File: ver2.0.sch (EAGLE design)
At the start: 57 parts

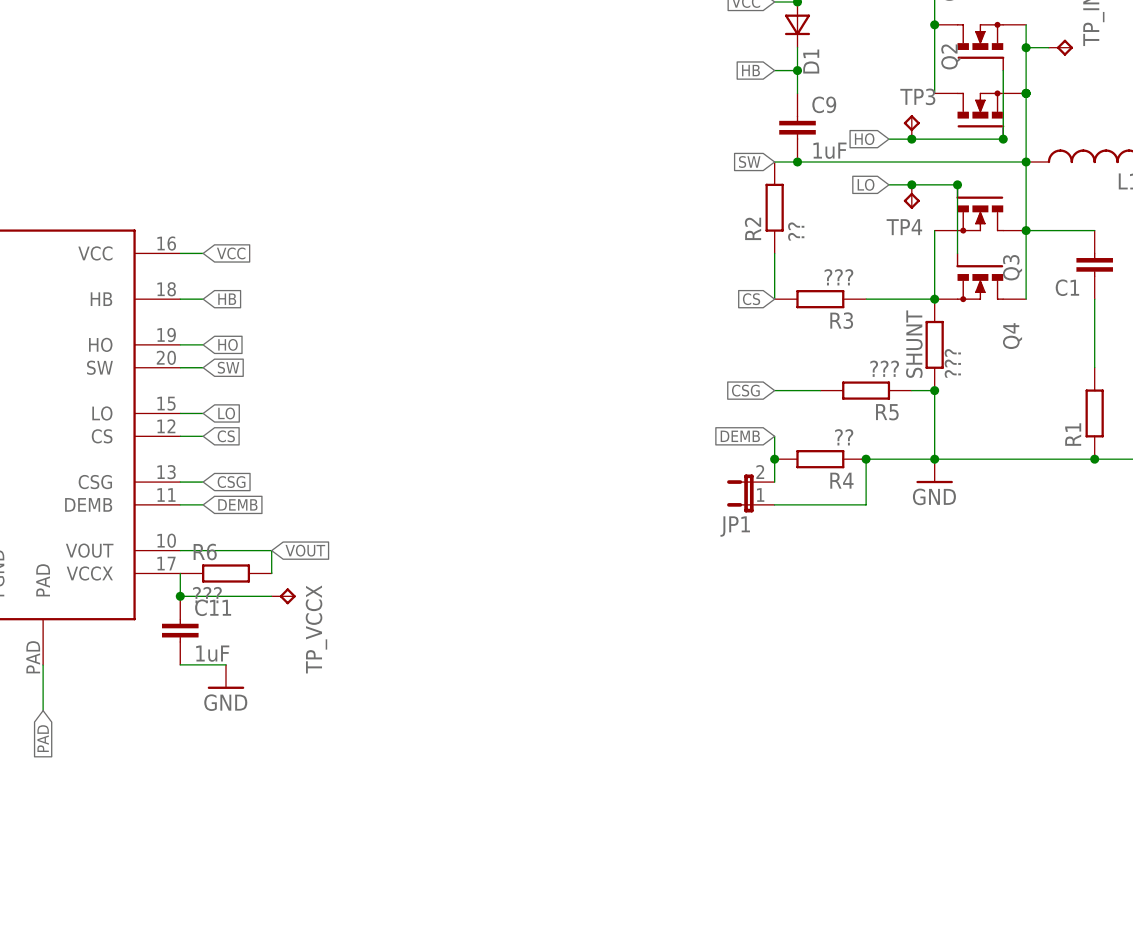
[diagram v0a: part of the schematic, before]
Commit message: 
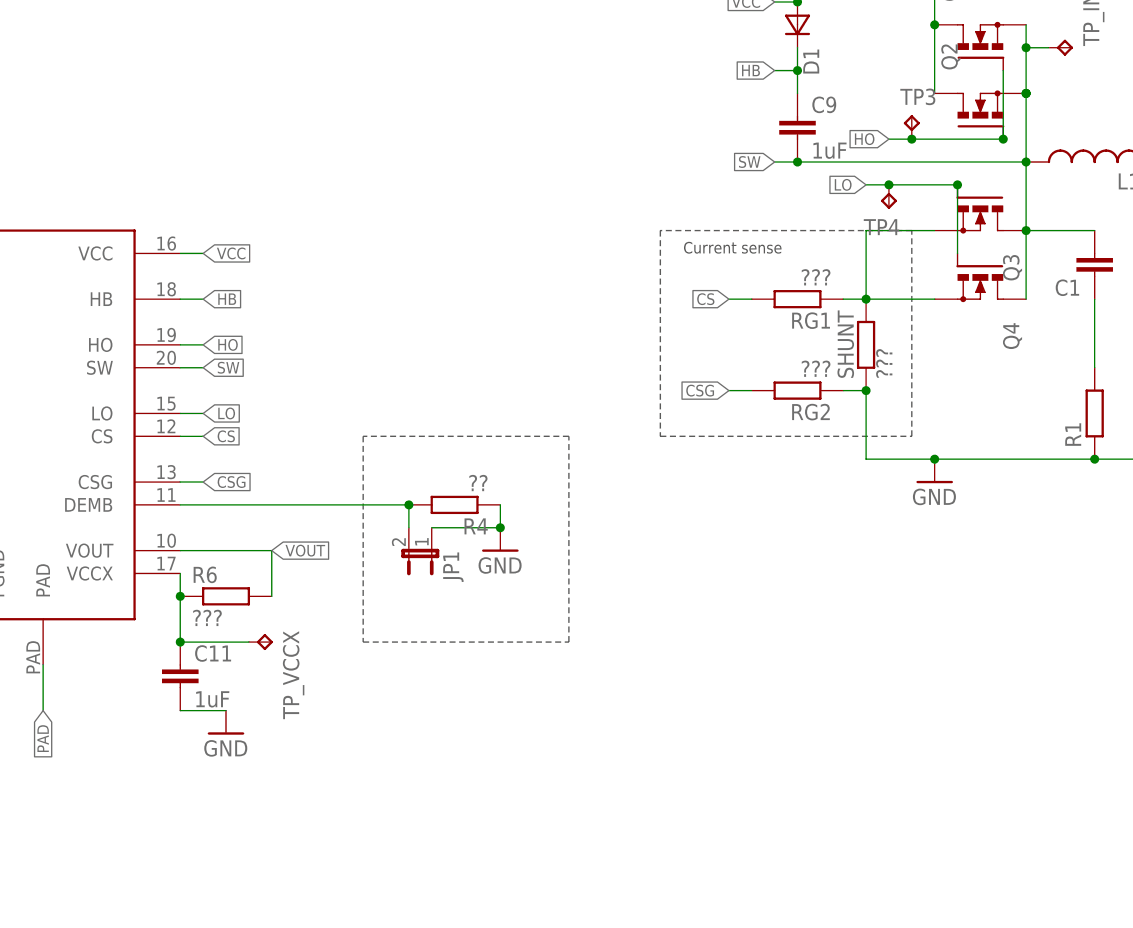
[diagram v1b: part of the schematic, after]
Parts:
- removed R2: ??, rcl:R-EU_R0603
- removed R3, R5: ???, rcl:R-EU_R0603
- added RG1, RG2: ???, rcl:R-EU_R0603
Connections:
- net CS: now also RG1.2; no longer R2.1, R3.2
- net CSG: now also RG2.2; no longer R5.2
- net GND: now also RG2.1; no longer R5.1
- net N$3: now also RG1.1; no longer R3.1
- net SW: no longer R2.2
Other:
- note added: "Current sense"
- moved on the sheet: C11, JP1, R4, R6, SHUNT, TP4, TP_VCCX
